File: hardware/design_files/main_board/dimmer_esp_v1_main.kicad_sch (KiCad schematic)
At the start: 54 parts, among them IC1 PEC11S-929K-S0015, J1 Screw_Terminal_01x03, J2 SM05B-SRSS-TB_LF__SN_, J3 Conn_01x02, K1 FTR-LYCA005Y, Q1 BC817, SW1 Commission, SW2 Toggle, SW3 Reset, U1 SGM2212-3.3XKC3G/TR, U2 USB TYPE-C 16PLT-H10.0, U3 SN74LV1T125DBVR, U4 ESP32-C6-MINI

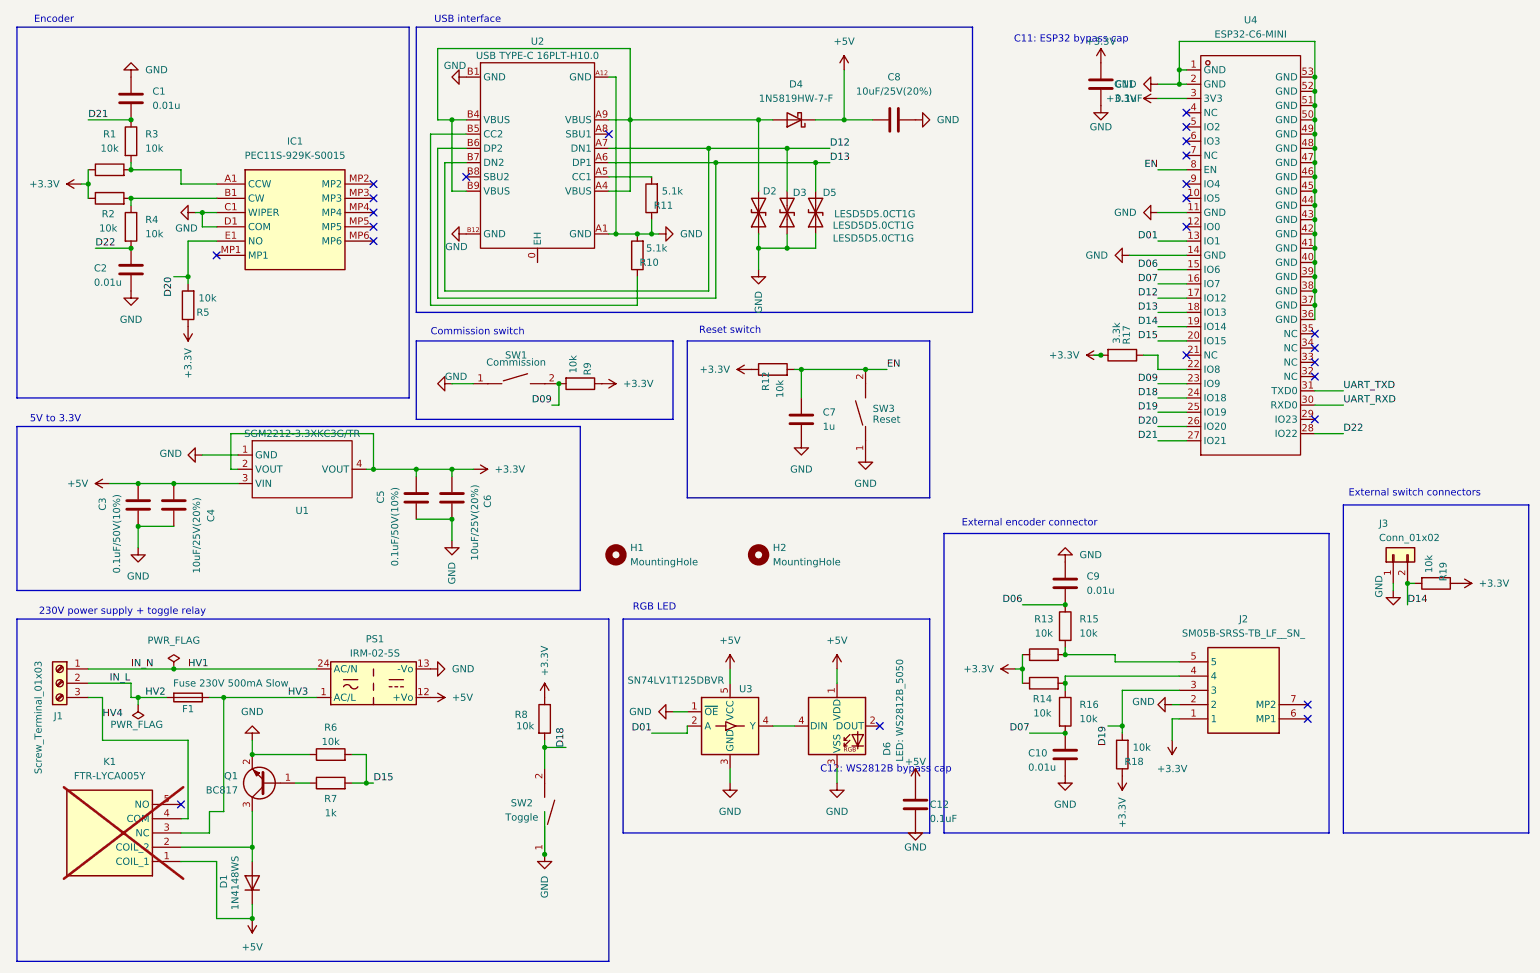
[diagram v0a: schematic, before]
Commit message: Add changes to PCB layout
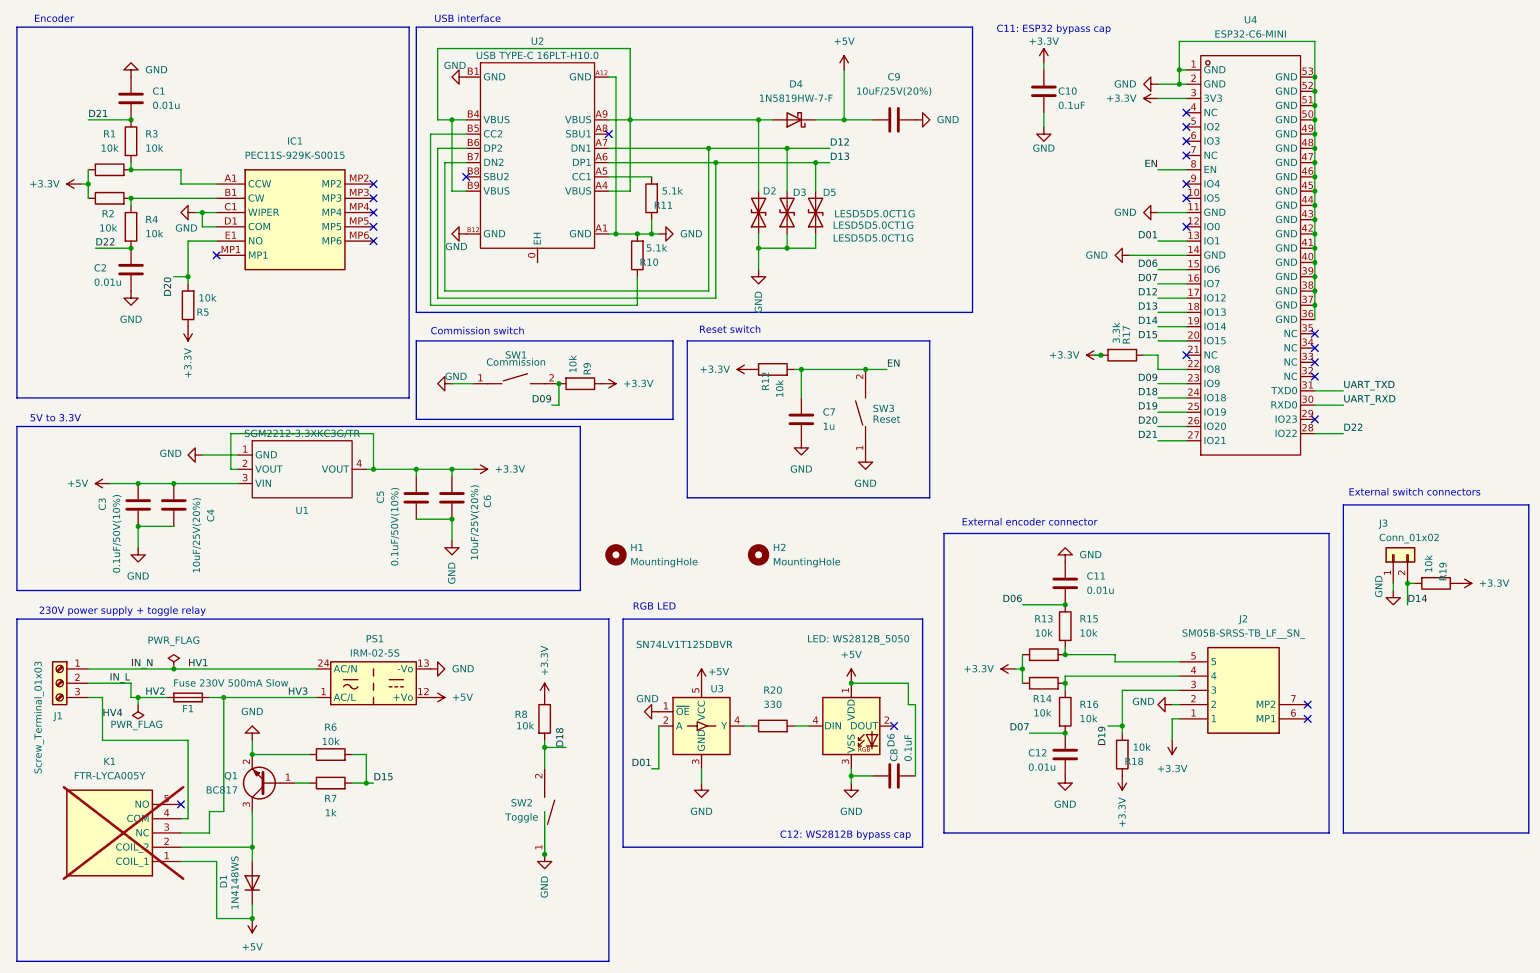
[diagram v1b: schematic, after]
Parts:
- added R20: 330, Resistor_SMD:R_0603_1608Metric, symbol Device:R
- renumbered C11 to C10, C9 to C11, C10 to C12, C12 to C8, C8 to C9
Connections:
- net +5V: now also C8.2; no longer C8.1
- net GND: now also C8.1; no longer C8.2
- net at U3.4 (Y): now also R20.1; no longer D6.4 (DIN)
- new net: D6.4 (DIN), R20.2
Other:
- moved on the sheet: C10, C8, D6, U3

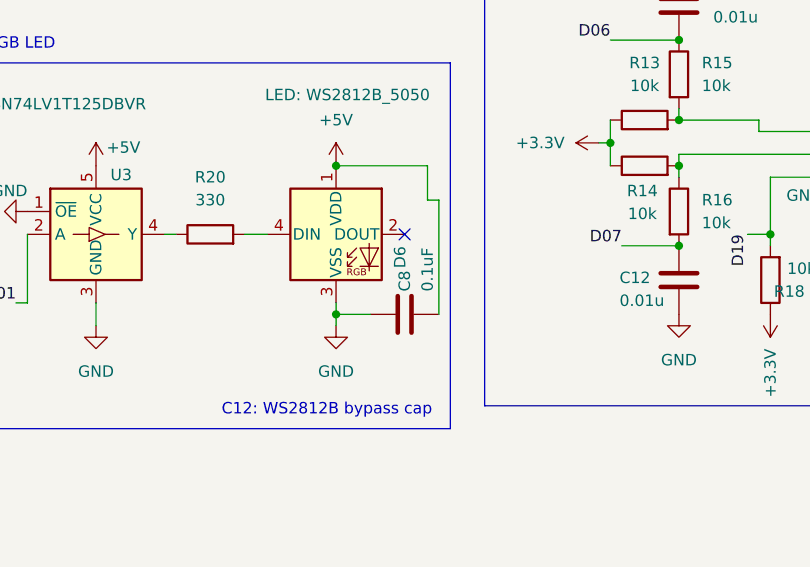
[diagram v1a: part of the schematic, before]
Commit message: Remove bypass cap for LED for now (no space on PCB)
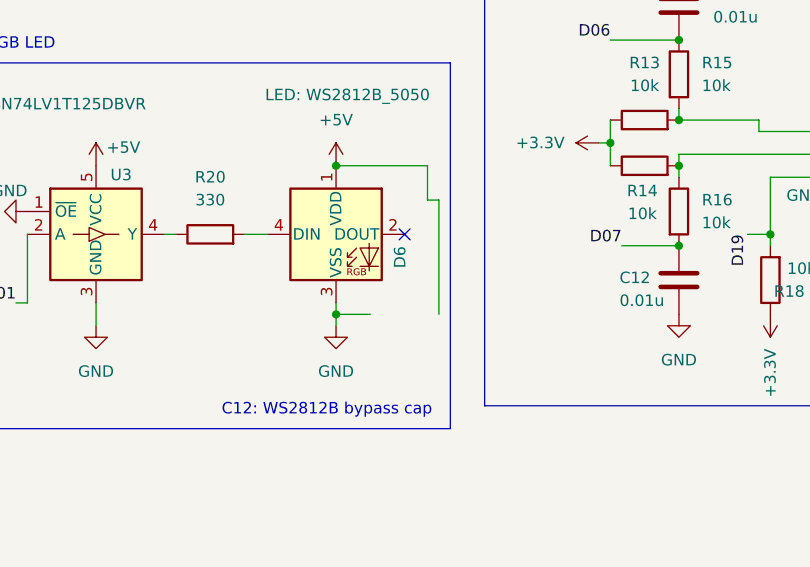
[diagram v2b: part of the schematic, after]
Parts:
- removed C8: 0.1uF, Capacitor_SMD:C_0603_1608Metric, symbol Device:C
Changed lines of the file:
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@@
-	)
-	(symbol
-		(lib_id "Device:C")
-		(at 171.45 151.13 90)
-		(unit 1)
-		(exclude_from_sim no)
-		(in_bom yes)
-		(on_board yes)
-		(dnp no)
-		(property "Reference" "C8"
-			(at 171.45 148.59 0)
-			(effects
-				(font
-					(size 1.27 1.27)
-				)
-				(justify left)
-			)
-		)
-		(property "Value" "0.1uF"
-			(at 173.99 148.59 0)
-			(effects
-				(font
-					(size 1.27 1.27)
-				)
-				(justify left)
-			)
-		)
-		(property "Footprint" "Capacitor_SMD:C_0603_1608Metric"
-			(at 175.26 150.1648 0)
-			(effects
-				(font
-					(size 1.27 1.27)
-				)
-				(hide yes)
-			)
-		)
-		(property "Datasheet" "~"
-			(at 171.45 151.13 0)
-			(effects
-				(font
-					(size 1.27 1.27)
-				)
-				(hide yes)
-			)
-		)
-		(property "Description" "WS2812B VDD bypass capacitor"
-			(at 171.45 151.13 0)
-			(effects
-				(font
-					(size 1.27 1.27)
-				)
-				(hide yes)
-			)
-		)
-		(property "LCSC" "C14663"
-			(at 171.45 151.13 0)
-			(effects
-				(font
-					(size 1.27 1.27)
-				)
-				(hide yes)
-			)
-		)
-		(pin "1"
-		)
-		(pin "2"
-		)
-		(instances
-			(project "dimmer_esp_v1_main"
-				(path "/ddfcd425-273c-4c73-9404-db5c5faab60e"
-					(reference "C8")
-					(unit 1)
-				)
-			)
-		)
 	)
 	(symbol

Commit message: Add MPN to components
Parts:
- C1, C11, C12, C2: MPN (none) -> 0603B103K500NT
- C10: MPN (none) -> CC0603KRX7R9BB104
- C3, C5: MPN (none) -> CT41G-0603-2X1-50V-0.1uF-K(N)
- C4, C6, C9: MPN (none) -> MVK25V10M4*5 4.0TP
- C7: MPN (none) -> CL10A105KB8NNNC
- D1: MPN (none) -> 1N4148WS
- D2, D3, D5: MPN (none) -> BNLESD5D5.0CT1G
- D4: MPN (none) -> 1N5819HW-7-F
- D6: MPN (none) -> XL-5050RGBC-2812B
- F1: MPN (none) -> 0443.500DR
- IC1: MPN (none) -> PEC11S-929K-S0015
- J1: MPN (none) -> 1715734
- J2: MPN (none) -> SM05B-SRSS-TB(LF)(SN)
- J3: MPN (none) -> SM02B-SRSS-TB(LF)(SN)
- PS1: MPN (none) -> IRM-02-5S
- Q1: MPN (none) -> BC817-40,215
- R1, R12, R13, R14, R15, R16, R18, R19, R2, R3, R4, R5, R6, R8, R9: MPN (none) -> 0603WAF1002T5E
- R10, R11: MPN (none) -> 0603WAF5101T5E
- R17: MPN (none) -> 0603WAF3301T5E
- R20: MPN (none) -> 0603WAF3300T5E
- R7: MPN (none) -> 0603WAF1001T5E
- SW1, SW2, SW3: MPN (none) -> TS-1088-AR02016
- U1: MPN (none) -> SGM2212-3.3XKC3G/TR
- U2: MPN (none) -> TYPE-C 16PLT-H10.0
- U3: MPN (none) -> SN74LV1T125DBVR
- U4: MPN (none) -> ESP32-C6-MINI-1-N4
